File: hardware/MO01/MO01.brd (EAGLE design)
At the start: 49 x 24.5 mm, 33 parts, among them J1 AUDIO-JACK2PTH, J2 M04X2, Q1 G2XX3---PW20, Q4 32.768 kHz, SW1 DTS-6

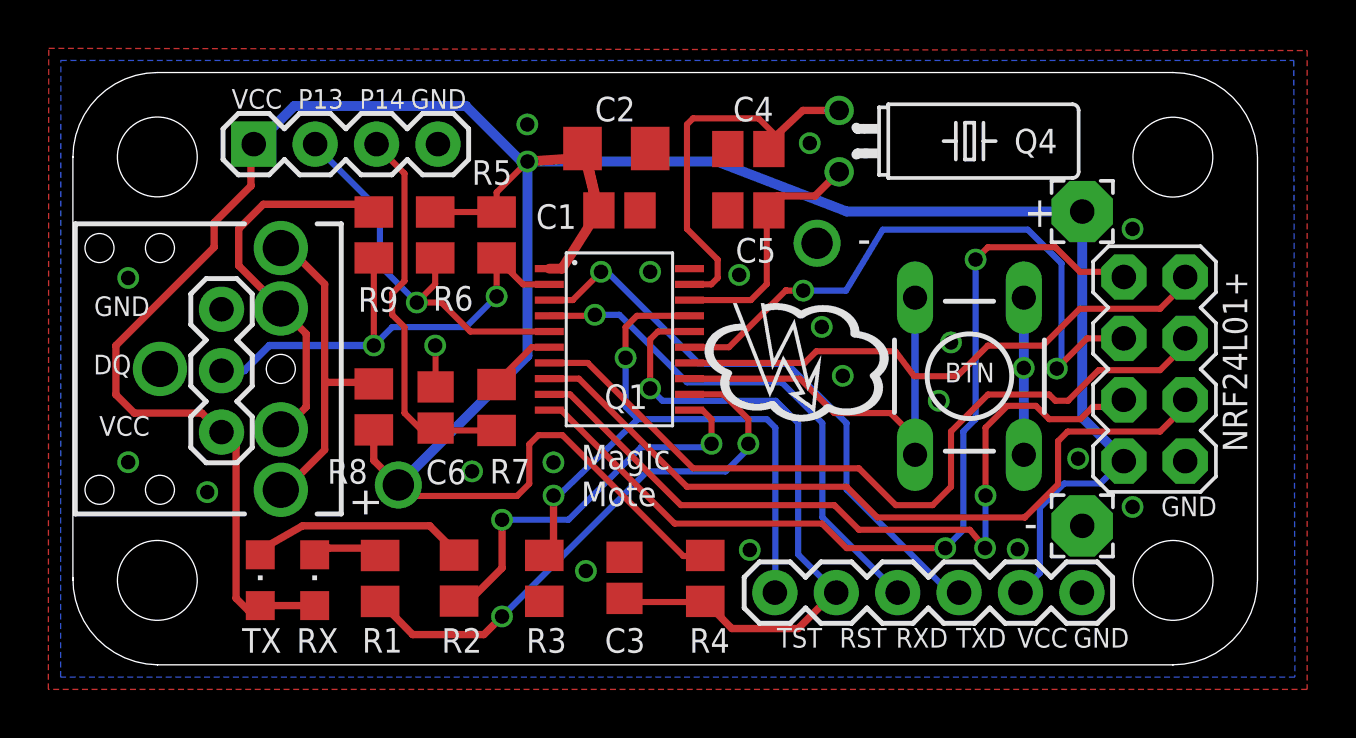
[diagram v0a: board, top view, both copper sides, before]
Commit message: panelized order from Elecrow
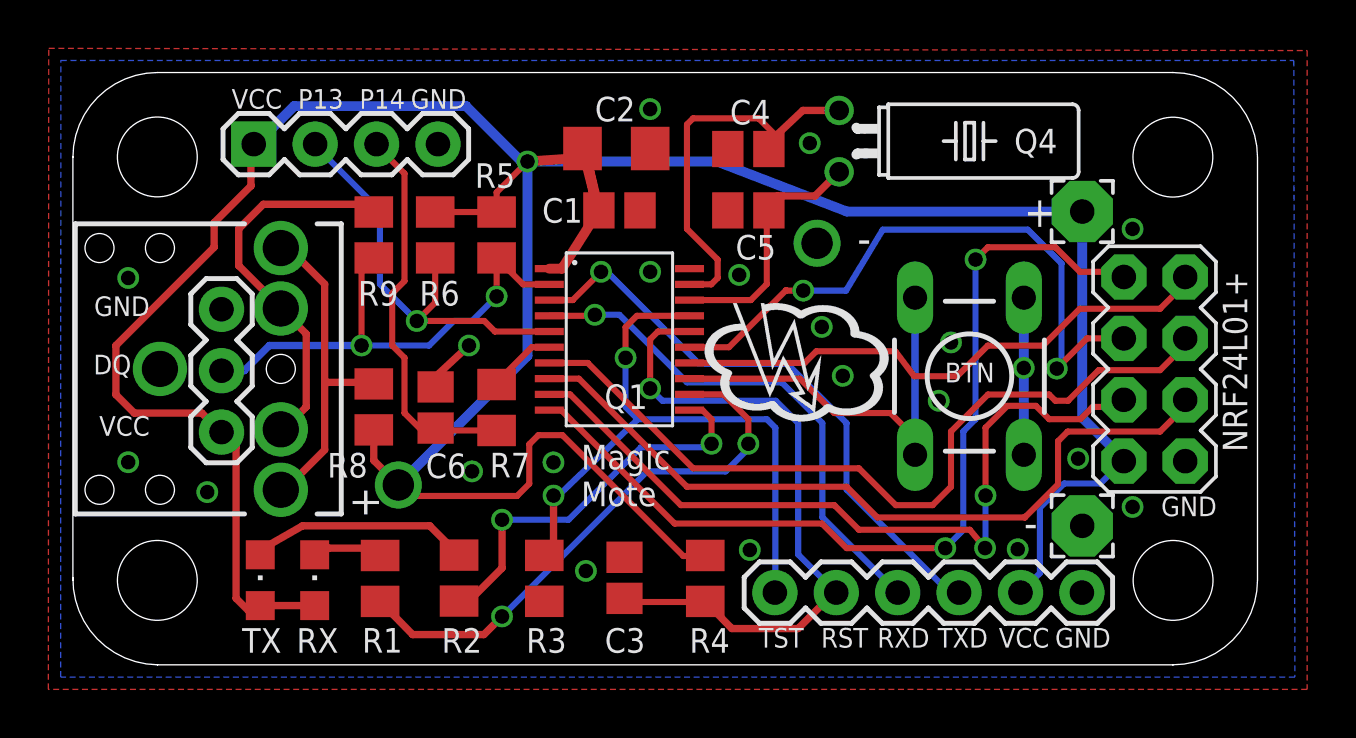
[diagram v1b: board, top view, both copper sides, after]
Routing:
- net P1.3: track 16.4 -> 17.6 mm
- net DQ: track 20.5 -> 21.4 mm
